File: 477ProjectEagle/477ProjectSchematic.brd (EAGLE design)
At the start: 101.6 x 127 mm, 78 parts, among them J1 POWER_JACK_BAT, J2 POWER_JACK_12VOUT, J3 RJ11-6PTH, Q1 AO4419, X1 22-23-2051, X10 MOTORS

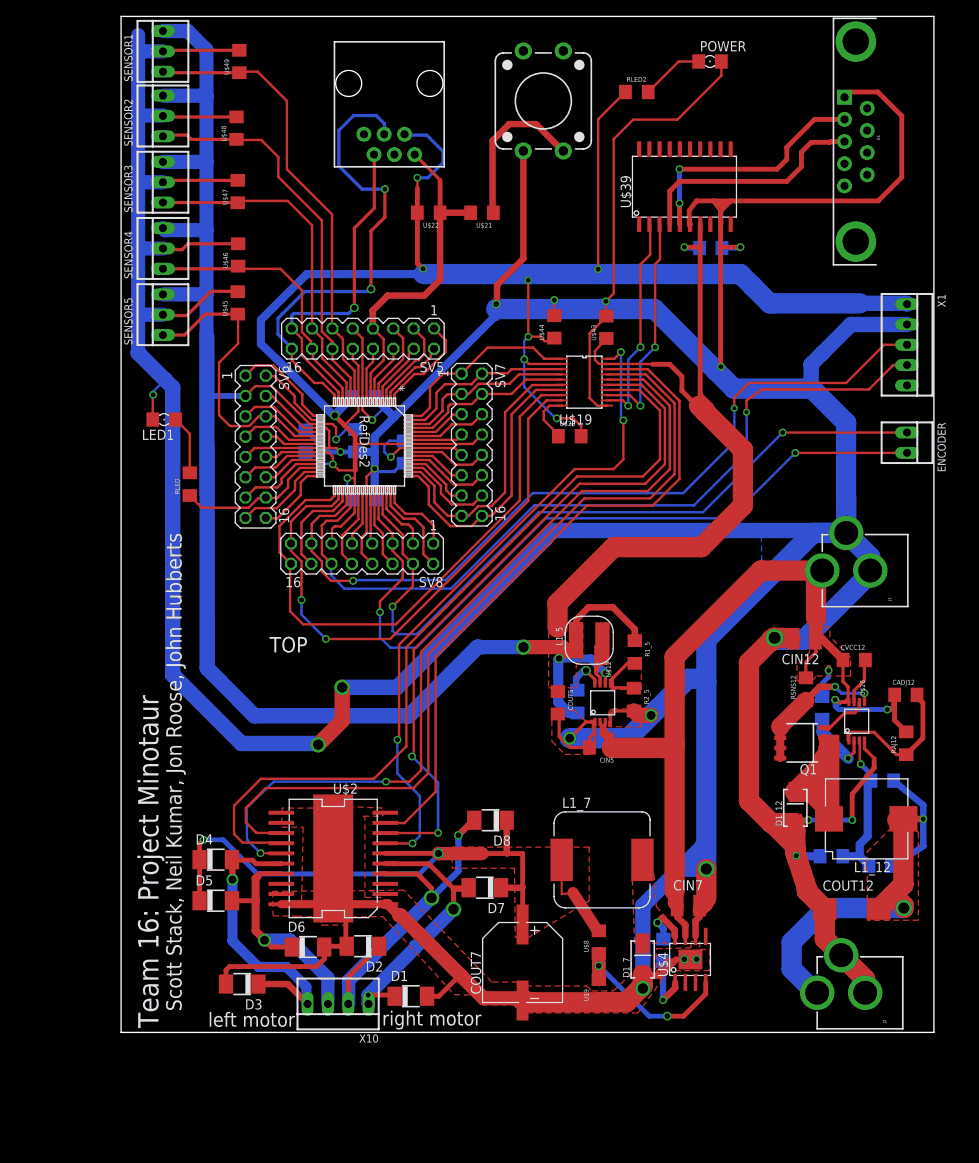
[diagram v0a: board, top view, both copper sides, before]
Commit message: Fixed some main PCB things
Put standoff holes in board. Fixed encoder headers so that there are 4
banks of 3 holed headers. (2 three holed headers per encoder.)
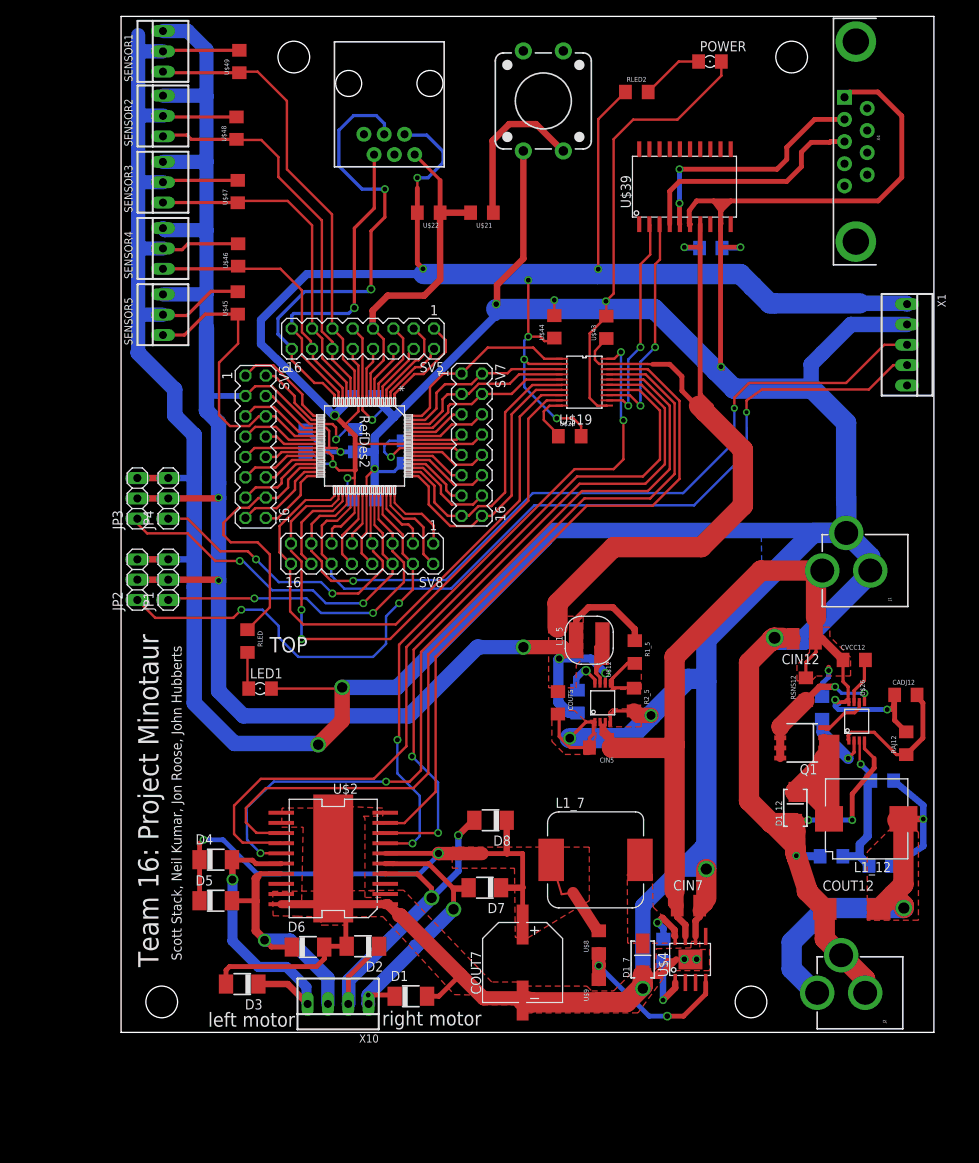
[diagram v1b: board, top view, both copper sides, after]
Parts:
- removed ENCODER: 22-23-2021, con-molex:22-23-2021
- added JP1, JP2, JP3, JP4: (no value), pinhead:1X03
- moved LED1 35.7 mm to (17.4, 43.0), turned to 0 degrees
- moved RLED 20.9 mm to (15.8, 48.9), turned to 270 degrees
- moved L1_7 0.81 mm to (59.3, 21.6)
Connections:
- removed net N$72: SV8.6, U$1.43
- new net N$12: JP3.1, SV8.6, U$1.43
- net +5V: now also JP1.2, JP2.2, JP3.2, JP4.2
- net GND: now also JP1.3, JP2.3, JP3.3, JP4.3
- net N$70: now also JP2.1; no longer ENCODER.1
- net N$71: now also JP1.1; no longer ENCODER.2
- net N$73: now also JP4.1
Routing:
- net N$71: track 97.2 -> 44.6 mm
- net N$12: track 0.00 -> 49.5 mm, vias 0 -> 2
- net N$70: track 95.0 -> 58.5 mm
- net N$73: track 6.66 -> 42.4 mm, vias 0 -> 2
- net GND: track 920.7 -> 946.7 mm, vias 19 -> 18
- net +5V: track 316.0 -> 338.3 mm, vias 5 -> 7
- net N$66: track 19.6 -> 34.4 mm
- net N$72: track 10.1 -> 0.00 mm
- net N$31: track 7.39 -> 4.58 mm
- net N$8: track 72.5 -> 74.3 mm

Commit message: Did some verification of the schematic
Fixed resistor values for power supplies. Fixed the max 233 chip
connections and the DB9 connections. Verified everything on the main PCB
schematic except reset button and programming header.
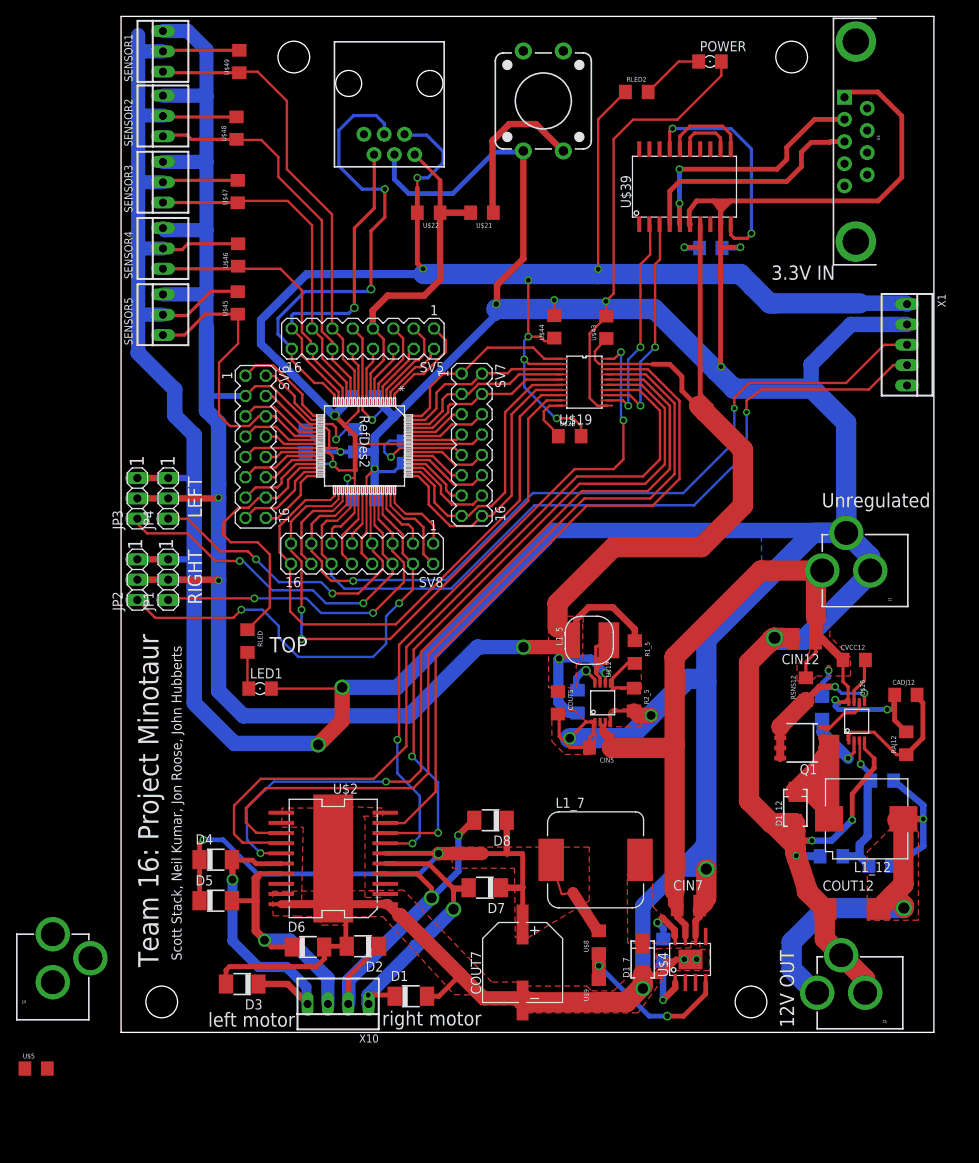
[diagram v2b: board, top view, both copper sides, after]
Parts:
- added J4: POWER_JACK_BAT, SparkFun-Connectors:POWER_JACK_PTH
- added U$5: 0.1uF, MinotaurParts:C1206
- CVCC12: value 740nF -> 470nF
- R1_5: value (none) -> 105k
- R2_5: value (none) -> 20k
- U$45, U$46, U$47, U$48, U$49: value 10uF -> 0.1uF
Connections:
- removed net N$86: J3.3
- new net N$13: U$39.V-, U$39.V-2
- new net N$62: U$39.C2-, U$39.C2-2
- new net N$72: U$39.C2+, U$39.C2+2
- net +3V3: now also J4.PWR
- net +7V: now also U$5.1
- net GND: now also J3.3, J4.GND, J4.GNDBREAK, U$4.2, U$5.2, X4.5; no longer X4.1
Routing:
- net N$13: track 0.00 -> 28.6 mm, vias 0 -> 2
- net GND: track 946.7 -> 969.4 mm
- net N$62: track 0.00 -> 10.8 mm
- net N$72: track 0.00 -> 7.17 mm
- net +5V: track 338.3 -> 339.8 mm
- net N$36: track 8.53 -> 9.18 mm
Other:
- board text added: "1"
- board text added: "12V OUT"
- board text added: "3.3V IN"
- board text added: "LEFT"
- board text added: "RIGHT"
- board text added: "Unregulated"

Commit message: PCB is almost finalized.
Scott Lab- Added bulk cap. added GND plane. Added lots of information on
the silkscreen. Barrel connectors for all power sources. Verified and
fixed programming header(added cap). Added barrel connectors to battery
PCB and made standoff drill holes.
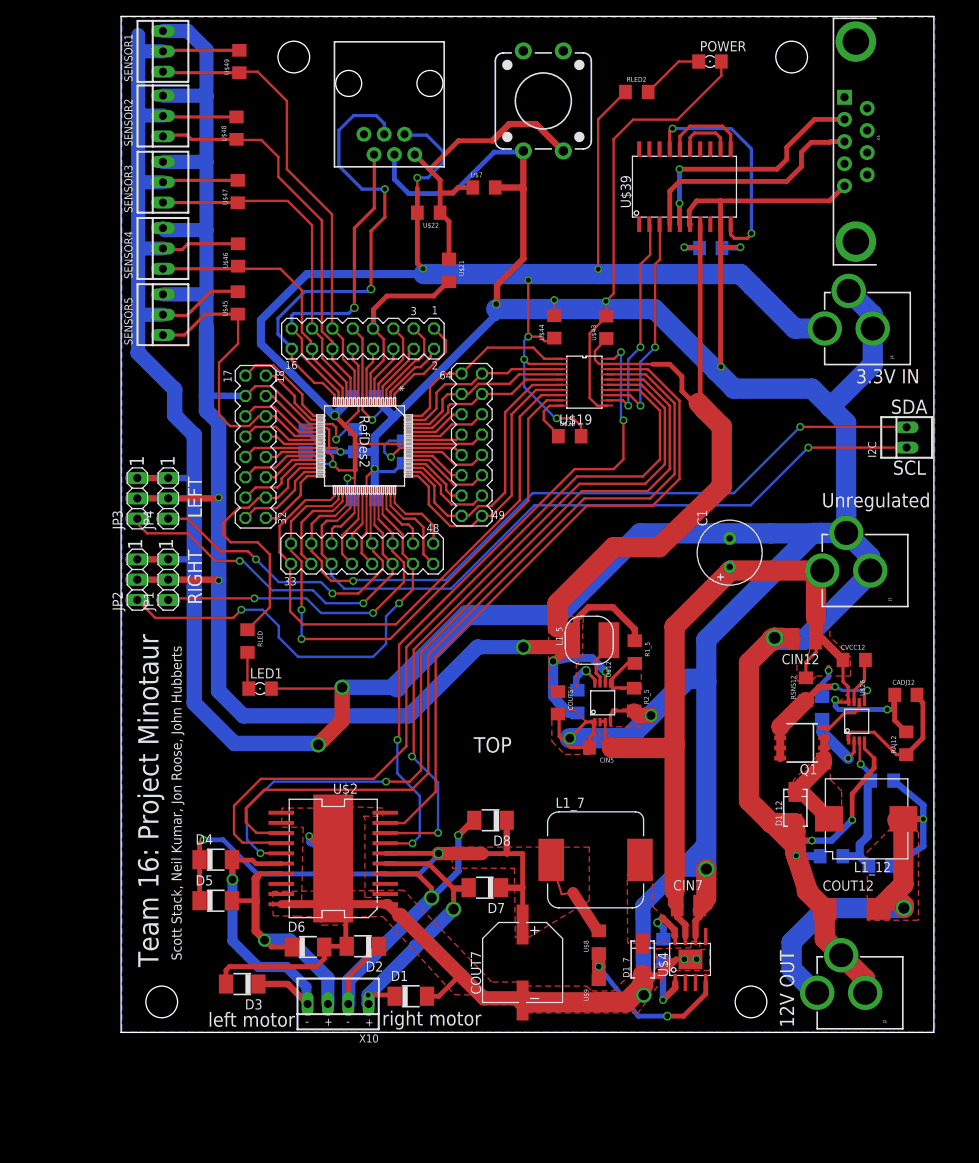
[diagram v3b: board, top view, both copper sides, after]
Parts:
- removed X1: 22-23-2051, con-molex:22-23-2051
- added C1: 100uF, rcl:E3,5-8
- added I2C: 22-23-2021, con-molex:22-23-2021
- added U$7: 0.1uF, MinotaurParts:C1206
- U$21: value 1k -> 470
- U$22: value 5k -> 10k
- moved J4 141.9 mm to (101.7, 88.0), turned to 90 degrees
- moved U$5 46.3 mm to (26.7, 23.0), flipped to the bottom
- moved U$21 8.30 mm to (41.0, 95.2), turned to 270 degrees
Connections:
- removed net N$60: SW_1.3, U$21.1
- new net N$79: SV5.7, U$1.7, U$21.2
- net +3V3: no longer X1.1
- net GND: now also C1.-, U$7.2; no longer X1.2
- net N$30: now also SW_1.3, U$21.1, U$7.1; no longer SV5.7, U$1.7, U$21.2
- net SCL: now also I2C.1; no longer X1.4
- net SDA: now also I2C.2; no longer X1.3
- net V+: now also C1.+
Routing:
- net N$79: track 0.00 -> 23.6 mm
- net N$60: track 20.1 -> 0.00 mm
- net +3V3: track 266.8 -> 256.8 mm
- net GND: track 969.4 -> 960.2 mm, vias 18 -> 21
- net SCL: track 101.3 -> 93.3 mm
- net SDA: track 102.7 -> 95.2 mm
- net V+: track 119.8 -> 126.7 mm
- net N$58: track 4.90 -> 0.00 mm
- net +5V: track 339.8 -> 334.9 mm
- net N$30: track 43.3 -> 39.6 mm
- net +7V: track 85.2 -> 88.4 mm
- net N$36: track 9.18 -> 6.28 mm
- net N$33: track 14.7 -> 13.9 mm
- net N$50: track 0.74 -> 0.00 mm
- net N$54: track 18.0 -> 18.6 mm
- added copper zone on layer 1, net N$33
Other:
- board text added: "+"
- board text added: "-"
- board text added: "16"
- board text added: "17"
- board text added: "18"
- board text added: "2"
- board text added: "3"
- board text added: "32"
- board text added: "33"
- board text added: "48"
- board text added: "49"
- board text added: "64"
- board text added: "SCL"
- board text added: "SDA"
